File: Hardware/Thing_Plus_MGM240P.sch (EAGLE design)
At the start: 67 parts, among them J1 THING_PLUS_LOGICAL, J2 USB Female Type C Connector, J3 QWIIC_RIGHT_ANGLE, J5 MICRO-SDFRICTION, Q1 20V/4.2A/52mΩ/1.4W, Q2 20V/4.2A/52mΩ/1.4W, U1 MGM240P, U2 XC6222B331MR-G, U4 MCP73831, U5 MAX17048, U6 MK22FN128VLH10

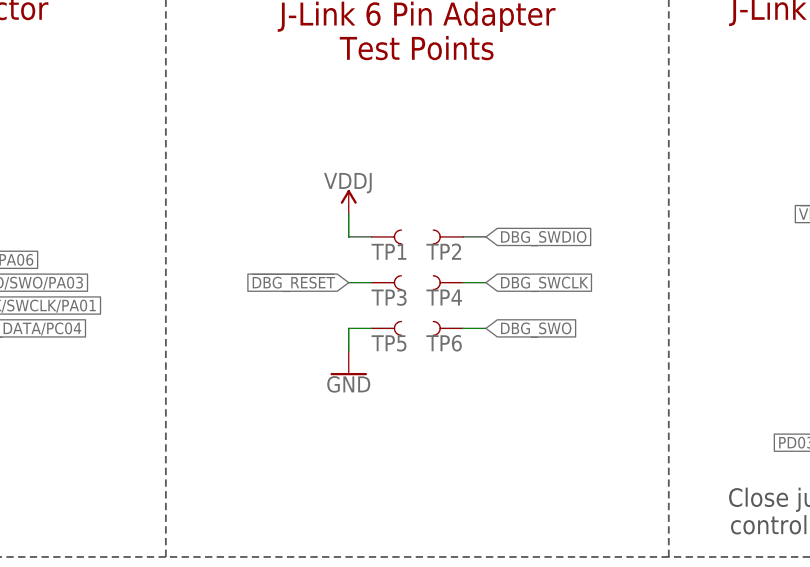
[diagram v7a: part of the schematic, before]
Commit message: Design review and checklist updates
Swap J-Link test points for new part
Change size of STAT silk and add pin number
Adjust fuel gauge cap position
Adjust board name silk positions
Add ordering instructions (4 layer board)
Improve GND continuity
Add layer numbers in copper
Move LED jumper out of standoff keepout
Update charge current silk labels to read "0.5A" instead of 500
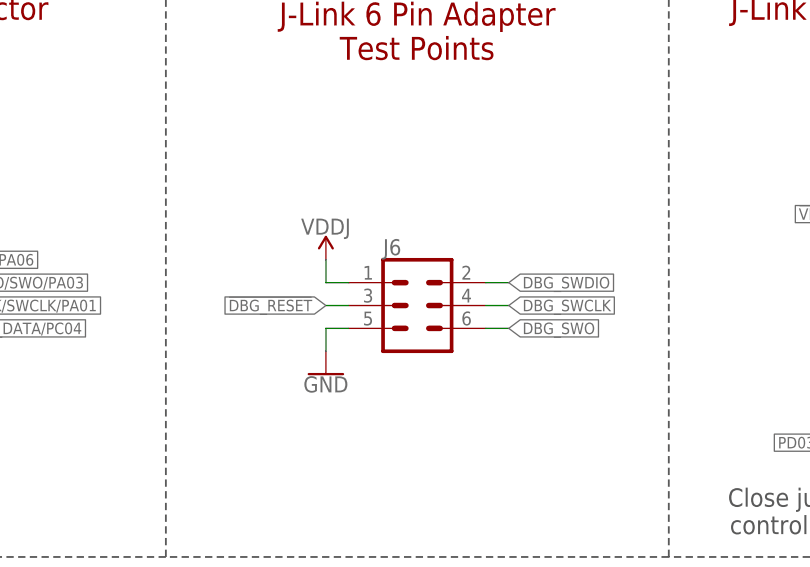
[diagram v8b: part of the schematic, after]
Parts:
- removed TP1, TP2, TP3, TP4, TP5, TP6: TEST-POINT3, SparkFun-Connectors:TEST-POINT3
- added J6: CONN_03X2, J_LINK_6_PIN:CONN_03X2
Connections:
- net !DBG_RESET!: now also J6.3; no longer TP3.1
- net DBG_SWCLK: now also J6.4; no longer TP4.1
- net DBG_SWDIO: now also J6.2; no longer TP2.1
- net DBG_SWO: now also J6.6; no longer TP6.1
- net GND: now also J6.5; no longer TP5.1
- net VDD: now also J6.1; no longer TP1.1
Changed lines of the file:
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@@
 <part name="J7" library="SparkFun-Connectors" deviceset="CONN_05X2" device="0.05_IN_PTH_SILK"/>
 <part name="GND11" library="SparkFun-PowerSymbols" deviceset="GND" device=""/>
-<part name="TP1" library="SparkFun-Connectors" deviceset="TEST-POINT" device="3" value="TEST-POINT3"/>
-<part name="TP2" library="SparkFun-Connectors" deviceset="TEST-POINT" device="3" value="TEST-POINT3"/>
-<part name="TP3" library="SparkFun-Connectors" deviceset="TEST-POINT" device="3" value="TEST-POINT3"/>
-<part name="TP4" library="SparkFun-Connectors" deviceset="TEST-POINT" device="3" value="TEST-POINT3"/>
-<part name="TP5" library="SparkFun-Connectors" deviceset="TEST-POINT" device="3" value="TEST-POINT3"/>
-<part name="TP6" library="SparkFun-Connectors" deviceset="TEST-POINT" device="3" value="TEST-POINT3"/>
 <part name="GND7" library="SparkFun-PowerSymbols" deviceset="GND" device=""/>
 <part name="C2" library="SparkFun-Capacitors" deviceset="0.1UF" device="-0402T-6.3V-10%-X7R" value="0.1uF"/>
@@
 <part name="SUPPLY31" library="SparkFun-PowerSymbols" deviceset="3.3V" device=""/>
 <part name="GND21" library="SparkFun-PowerSymbols" deviceset="GND" device=""/>
+<part name="J6" library="J_LINK_6_PIN" deviceset="CONN_03X2" device=""/>
 </parts>
 <sheets>
@@
 <attribute name="VALUE" x="198.12" y="169.926" size="1.778" layer="96" align="top-center"/>
 </instance>
-<instance part="TP1" gate="G$1" x="246.38" y="185.42" smashed="yes">
-<attribute name="NAME" x="246.38" y="182.88" size="1.778" layer="95" font="vector"/>
-</instance>
-<instance part="TP2" gate="G$1" x="256.54" y="185.42" smashed="yes" rot="MR0">
-<attribute name="NAME" x="256.54" y="182.88" size="1.778" layer="95" font="vector" rot="MR0"/>
-</instance>
-<instance part="TP3" gate="G$1" x="246.38" y="180.34" smashed="yes">
-<attribute name="NAME" x="246.38" y="177.8" size="1.778" layer="95" font="vector"/>
-</instance>
-<instance part="TP4" gate="G$1" x="256.54" y="180.34" smashed="yes" rot="MR0">
-<attribute name="NAME" x="256.54" y="177.8" size="1.778" layer="95" font="vector" rot="MR0"/>
-</instance>
-<instance part="TP5" gate="G$1" x="246.38" y="175.26" smashed="yes">
-<attribute name="NAME" x="246.38" y="172.72" size="1.778" layer="95" font="vector"/>
-</instance>
-<instance part="TP6" gate="G$1" x="256.54" y="175.26" smashed="yes" rot="MR0">
-<attribute name="NAME" x="256.54" y="172.72" size="1.778" layer="95" font="vector" rot="MR0"/>
-</instance>
-<instance part="GND7" gate="1" x="243.84" y="170.18" smashed="yes">
-<attribute name="VALUE" x="243.84" y="169.926" size="1.778" layer="96" align="top-center"/>
+<instance part="GND7" gate="1" x="241.3" y="170.18" smashed="yes">
+<attribute name="VALUE" x="241.3" y="169.926" size="1.778" layer="96" align="top-center"/>
 </instance>
 <instance part="C2" gate="G$1" x="12.7" y="121.92" smashed="yes">
@@
 <attribute name="VALUE" x="238.76" y="63.754" size="1.778" layer="96" align="bottom-center"/>
 </instance>
-<instance part="SUPPLY12" gate="VDD" x="243.84" y="187.96" smashed="yes">
-<attribute name="VALUE" x="243.84" y="190.754" size="1.778" layer="96" align="bottom-center"/>
+<instance part="SUPPLY12" gate="VDD" x="241.3" y="182.88" smashed="yes">
+<attribute name="VALUE" x="241.3" y="185.674" size="1.778" layer="96" align="bottom-center"/>
 </instance>
 <instance part="Q2" gate="G$1" x="307.34" y="195.58" smashed="yes" rot="MR90">
@@
 <instance part="GND21" gate="1" x="109.22" y="175.26" smashed="yes">
 <attribute name="VALUE" x="109.22" y="175.006" size="1.778" layer="96" align="top-center"/>
+</instance>
+<instance part="J6" gate="G$1" x="251.46" y="177.8" smashed="yes">
+<attribute name="NAME" x="247.65" y="183.388" size="1.778" layer="95" font="vector"/>
 </instance>
 </instances>
@@
 </segment>
 <segment>
-<pinref part="TP5" gate="G$1" pin="1"/>
-<wire x1="246.38" y1="175.26" x2="243.84" y2="175.26" width="0.1524" layer="91"/>
-<wire x1="243.84" y1="175.26" x2="243.84" y2="172.72" width="0.1524" layer="91"/>
-<pinref part="GND7" gate="1" pin="GND"/>
-</segment>
-<segment>
 <pinref part="GND12" gate="1" pin="GND"/>
 <pinref part="C2" gate="G$1" pin="2"/>
@@
 <pinref part="C1" gate="G$1" pin="2"/>
 <wire x1="109.22" y1="177.8" x2="109.22" y2="180.34" width="0.1524" layer="91"/>
+</segment>
+<segment>
+<pinref part="J6" gate="G$1" pin="5"/>
+<wire x1="243.84" y1="175.26" x2="241.3" y2="175.26" width="0.1524" layer="91"/>
+<pinref part="GND7" gate="1" pin="GND"/>
+<wire x1="241.3" y1="175.26" x2="241.3" y2="172.72" width="0.1524" layer="91"/>
 </segment>
 </net>
@@
 </segment>
 <segment>
-<pinref part="TP4" gate="G$1" pin="1"/>
-<wire x1="256.54" y1="180.34" x2="259.08" y2="180.34" width="0.1524" layer="91"/>
-<label x="259.08" y="180.34" size="1.27" layer="95" font="vector" xref="yes"/>
+<pinref part="J6" gate="G$1" pin="4"/>
+<wire x1="259.08" y1="177.8" x2="261.62" y2="177.8" width="0.1524" layer="91"/>
+<label x="261.62" y="177.8" size="1.27" layer="95" xref="yes"/>
 </segment>
 </net>
@@
 </segment>
 <segment>
-<pinref part="TP6" gate="G$1" pin="1"/>
-<wire x1="256.54" y1="175.26" x2="259.08" y2="175.26" width="0.1524" layer="91"/>
-<label x="259.08" y="175.26" size="1.27" layer="95" font="vector" xref="yes"/>
+<pinref part="J6" gate="G$1" pin="6"/>
+<wire x1="259.08" y1="175.26" x2="261.62" y2="175.26" width="0.1524" layer="91"/>
+<label x="261.62" y="175.26" size="1.27" layer="95" xref="yes"/>
 </segment>
 </net>
@@
 </segment>
 <segment>
-<pinref part="TP3" gate="G$1" pin="1"/>
-<wire x1="246.38" y1="180.34" x2="243.84" y2="180.34" width="0.1524" layer="91"/>
-<label x="243.84" y="180.34" size="1.27" layer="95" font="vector" rot="R180" xref="yes"/>
+<pinref part="J6" gate="G$1" pin="3"/>
+<wire x1="243.84" y1="177.8" x2="241.3" y2="177.8" width="0.1524" layer="91"/>
+<label x="241.3" y="177.8" size="1.27" layer="95" rot="R180" xref="yes"/>
 </segment>
 </net>
 <net name="DBG_SWDIO" class="0">
-<segment>
-<pinref part="TP2" gate="G$1" pin="1"/>
-<wire x1="256.54" y1="185.42" x2="259.08" y2="185.42" width="0.1524" layer="91"/>
-<label x="259.08" y="185.42" size="1.27" layer="95" font="vector" xref="yes"/>
-</segment>
 <segment>
 <pinref part="U6" gate="G$1" pin="PTA3"/>
 <wire x1="256.54" y1="60.96" x2="254" y2="60.96" width="0.1524" layer="91"/>
 <label x="254" y="60.96" size="1.27" layer="95" font="vector" rot="R180" xref="yes"/>
+</segment>
+<segment>
+<pinref part="J6" gate="G$1" pin="2"/>
+<wire x1="259.08" y1="180.34" x2="261.62" y2="180.34" width="0.1524" layer="91"/>
+<label x="261.62" y="180.34" size="1.27" layer="95" xref="yes"/>
 </segment>
 </net>
@@
 </segment>
 <segment>
-<pinref part="TP1" gate="G$1" pin="1"/>
-<wire x1="246.38" y1="185.42" x2="243.84" y2="185.42" width="0.1524" layer="91"/>
-<wire x1="243.84" y1="185.42" x2="243.84" y2="187.96" width="0.1524" layer="91"/>
-<pinref part="SUPPLY12" gate="VDD" pin="VDD"/>
-</segment>
-<segment>
 <pinref part="Q2" gate="G$1" pin="D"/>
 <wire x1="312.42" y1="198.12" x2="314.96" y2="198.12" width="0.1524" layer="91"/>
@@
 <wire x1="314.96" y1="198.12" x2="314.96" y2="200.66" width="0.1524" layer="91"/>
 </segment>
-</net>
+<segment>
+<pinref part="J6" gate="G$1" pin="1"/>
+<wire x1="243.84" y1="180.34" x2="241.3" y2="180.34" width="0.1524" layer="91"/>
+<pinref part="SUPPLY12" gate="VDD" pin="VDD"/>
+<wire x1="241.3" y1="180.34" x2="241.3" y2="182.88" width="0.1524" layer="91"/>
+</segment>
+</net>
